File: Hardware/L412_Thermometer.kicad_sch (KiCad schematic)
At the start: 22 parts, among them J1 USB_B_Mini, J2 Conn_01x03, J3 Conn_Si7021, J4 Conn_LCD, J5 Debug, J6 Serial, U1 AP7343D-33W5, U2 STM32L412KBTx, Y1 ABS07 [9pF, 32.768kHz]

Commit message: PCB updated
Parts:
- added C10, C9: 100n, Capacitor_SMD:C_0603_1608Metric, symbol Device:C
- added SW1, SW2: SW_Push, Button_Switch_THT:SW_PUSH_6mm, symbol Switch:SW_Push
- C8: renamed from C?; footprint (none) -> Capacitor_SMD:C_0603_1608Metric
- J2: value Conn_01x03 -> Power
- J3: value Conn_Si7021 -> Si7021
- Q1: renamed from Q?; footprint (none) -> Package_TO_SOT_SMD:SOT-323_SC-70
- R2, R3, R4: renamed from R?; footprint (none) -> Resistor_SMD:R_0603_1608Metric
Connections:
- net GND: now also C10.2, C9.2, SW1.1, SW2.1
- net BAT_MEAS_EN: now reaches U2.29 (PB6)
- net BAT_MEAS_EN: now also Q1.1 (G), R2.2
- net SCREEN: now reaches U2.30 (PB7)
- net SCREEN: now also C10.1, SW2.2
- removed net BAT_MEAS: Q1.1 (G), R2.2, U2.7 (PA1)
- net VBAT renamed V_BAT
- net V_BAT: now also U2.7 (PA1); no longer U2.6 (PA0)
- new net WKUP: C9.1, SW1.2, U2.6 (PA0)
- no-connect marks 9 -> 7
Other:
- moved on the sheet: C8, J1, J2, J3, Q1, R2, R3, R4, U2

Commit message: Routed PCB
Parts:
- added C11: 4u7, Capacitor_Tantalum_SMD:CP_EIA-1608-10_AVX-L, symbol Device:C_Polarized
- added R5, R6, R7: 62R, Resistor_SMD:R_0603_1608Metric, symbol Device:R_Small
- SW1, SW2: footprint Button_Switch_THT:SW_PUSH_6mm -> Button_Switch_SMD:SW_SPST_SKQG_WithStem
- U1: value AP7343D-33W5 -> ?
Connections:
- net +5V: now also C11.1
- net GND: now also C11.2
- net NRST: now also R7.1; no longer J5.2 (Pin_2)
- net SCREEN: now also U2.18 (PA8); no longer U2.30 (PB7)
- net SWCLK: now also R6.1; no longer J5.3 (Pin_3)
- net SWDIO: now also R5.1; no longer J5.4 (Pin_4)
- net +3V3 renamed +3V0
- new net: J5.2 (Pin_2), R7.2
- new net: J5.3 (Pin_3), R6.2
- new net: J5.4 (Pin_4), R5.2
- no-connect marks 7 -> 9
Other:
- moved on the sheet: C1, C2, C3

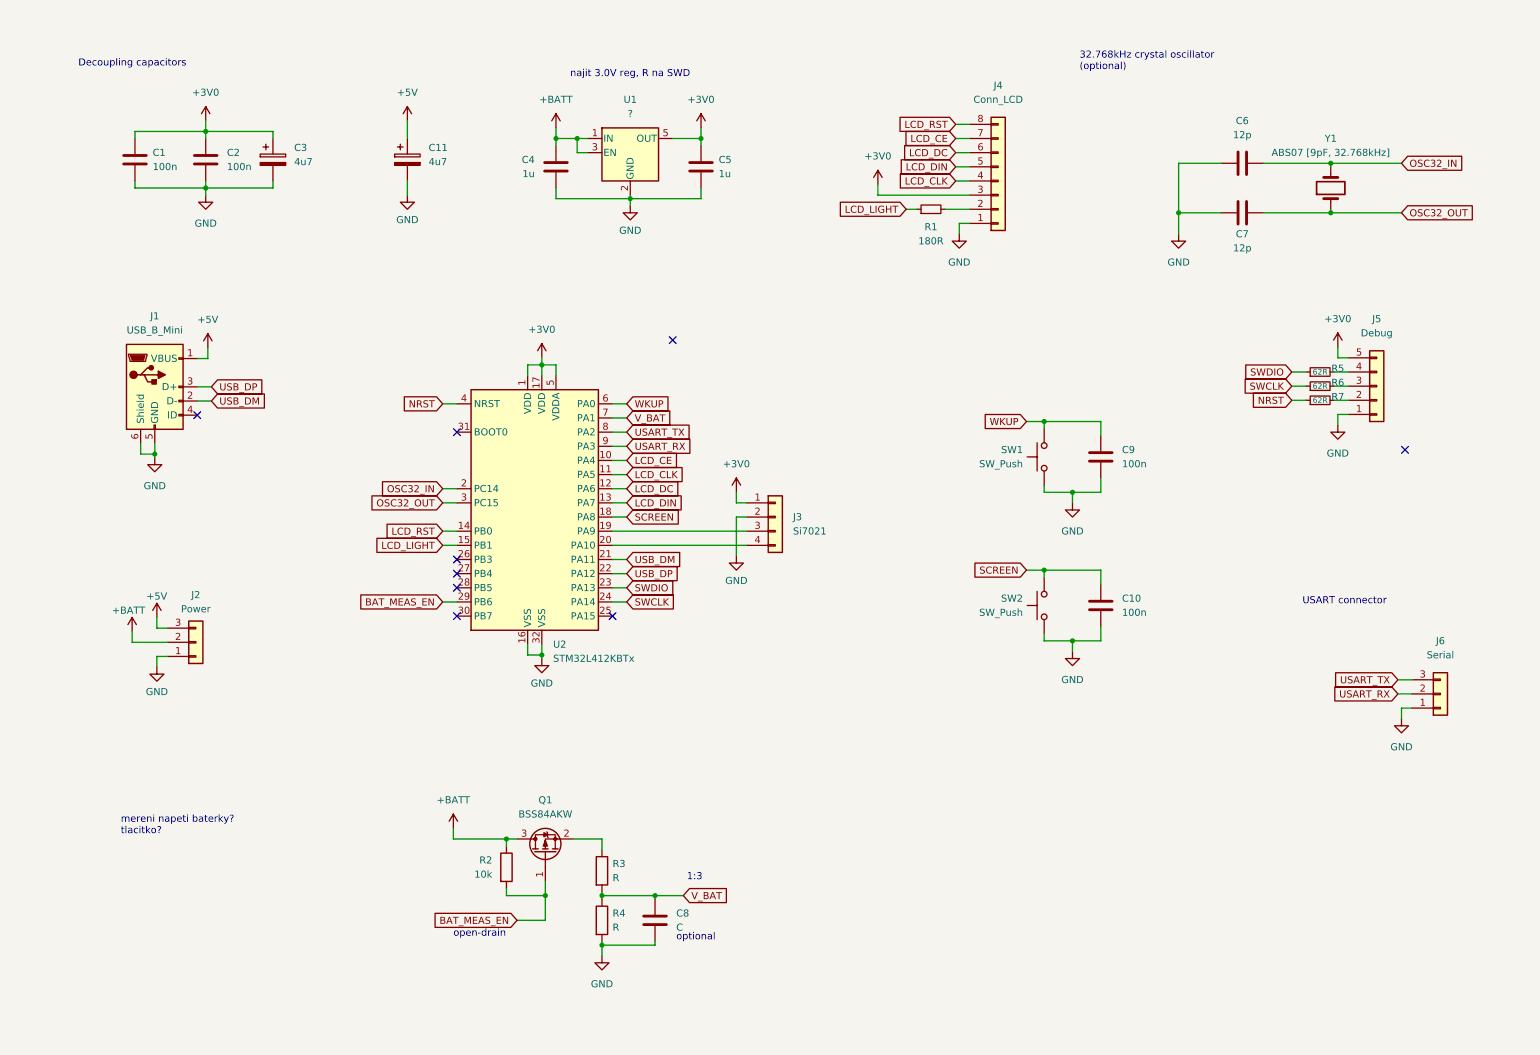
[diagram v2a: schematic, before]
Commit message: Voltage divider values, changed footprint of P-MOS, picked a voltage regulator
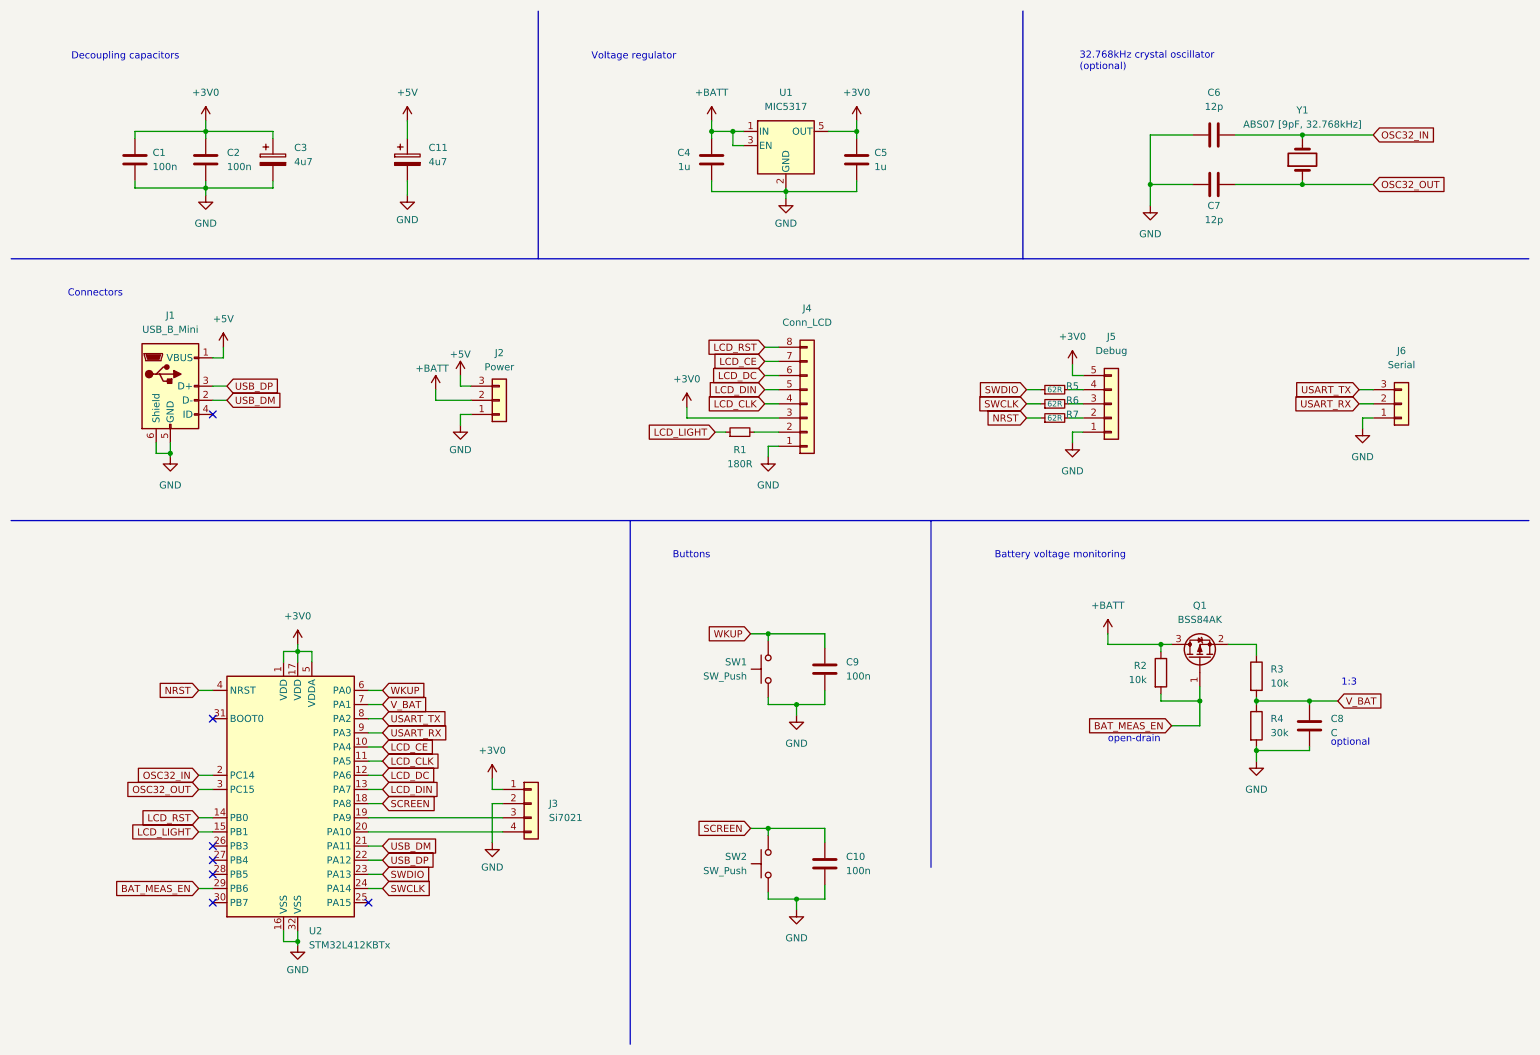
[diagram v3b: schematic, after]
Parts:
- Q1: value BSS84AKW -> BSS84AK; footprint Package_TO_SOT_SMD:SOT-323_SC-70 -> Package_TO_SOT_SMD:SOT-23
- R3: value R -> 10k
- R4: value R -> 30k
- U1: value ? -> MIC5317
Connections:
- no-connect marks 9 -> 7
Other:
- note added: "Battery voltage monitoring"
- note added: "Buttons"
- note added: "Connectors"
- note added: "Voltage regulator"
- note removed: "USART connector"
- note removed: "mereni napeti baterky? tlacitko?"
- note removed: "najit 3.0V reg, R na SWD"
- moved on the sheet: C10, C4, C5, C6, C7, C8, C9, J1, J2, J3, J4, J5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
